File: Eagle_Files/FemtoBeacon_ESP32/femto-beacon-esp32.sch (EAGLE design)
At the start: 64 parts, among them IC1 FT232RQ

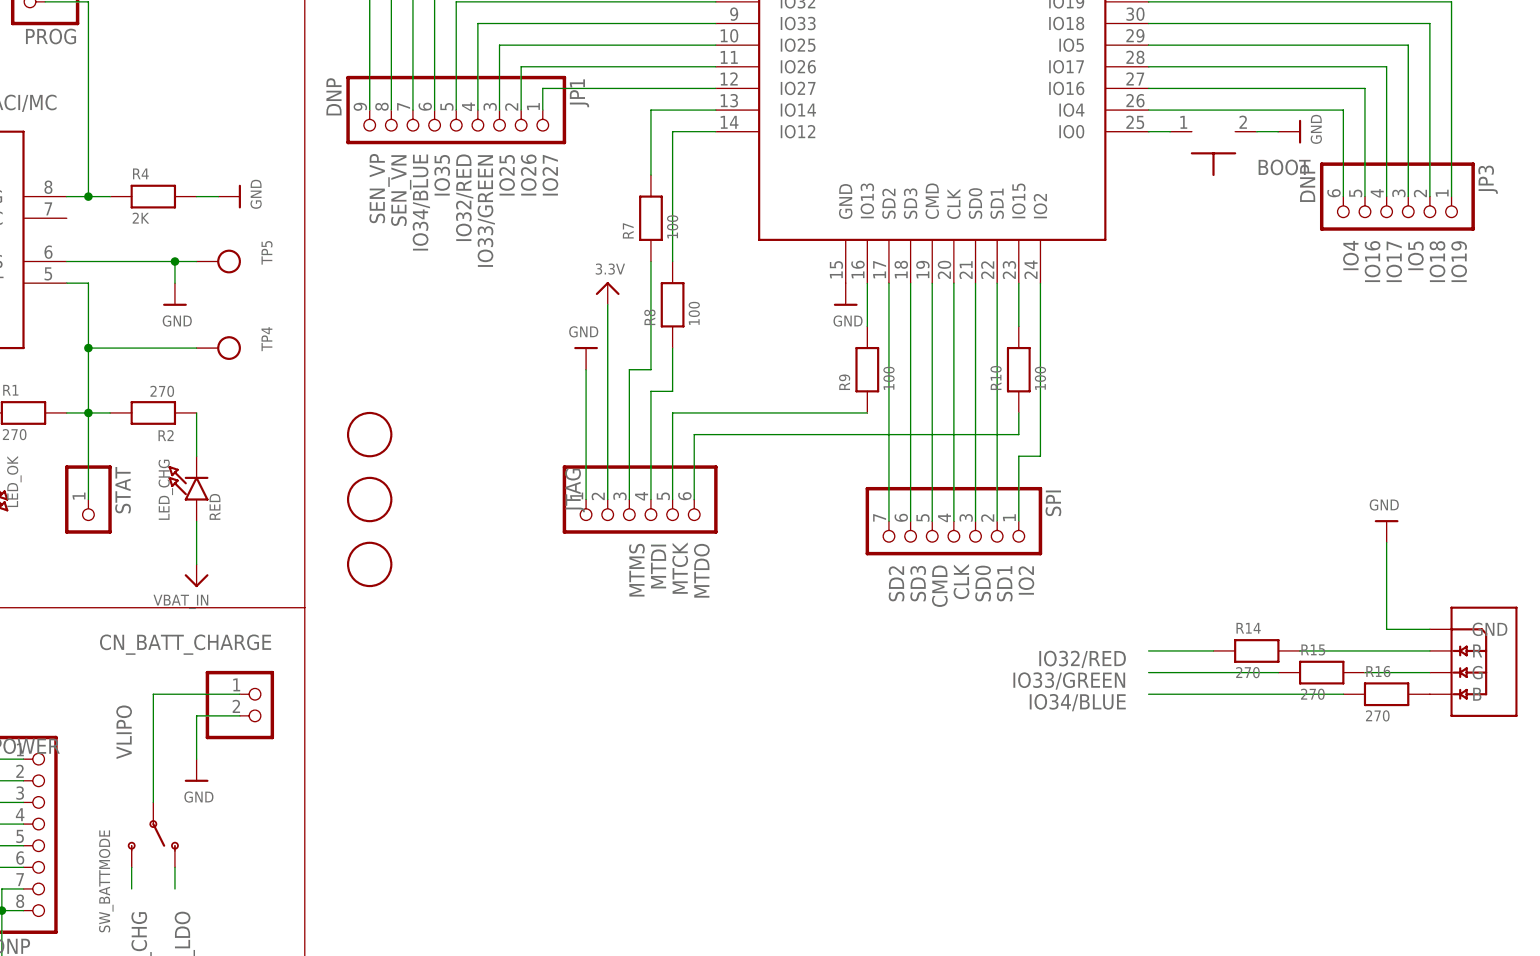
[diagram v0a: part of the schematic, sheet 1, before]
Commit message: Updating ESP32-WROOM-32 board. RGB Blue pin reassigned, and RGB pin 1 set to VCC instead of GND. LiPo connector pins were switched, corrected now.
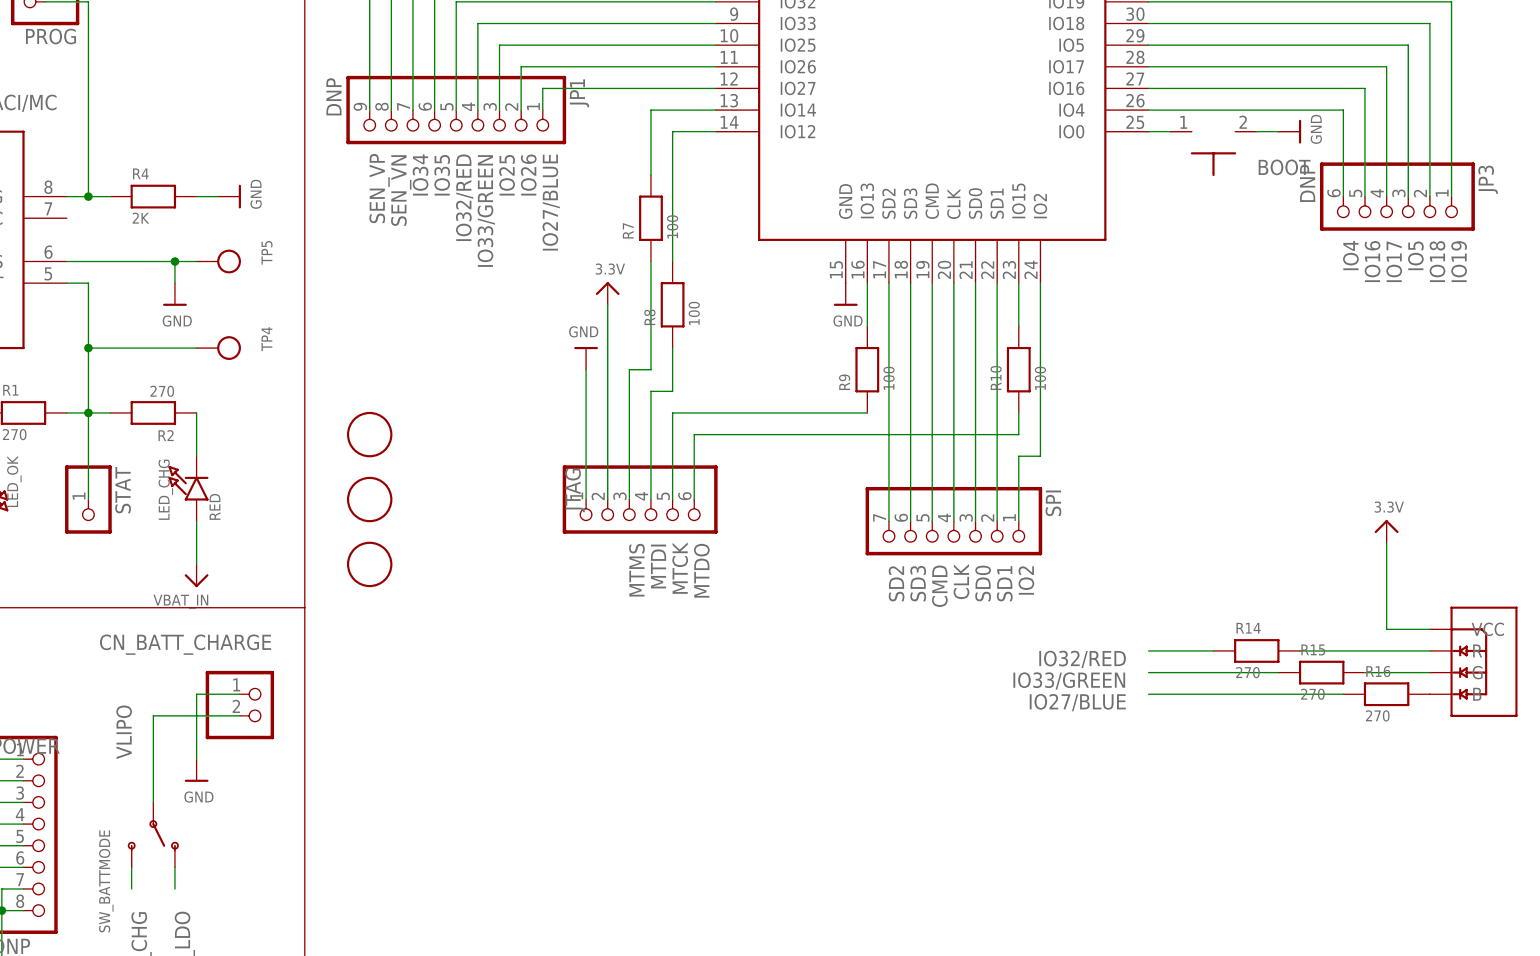
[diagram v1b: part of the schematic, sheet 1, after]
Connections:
- removed net IO27: JP1.1, MOD1.IO27
- removed net IO34/BLUE: JP1.7, MOD1.IO34, R16.1
- new net IO27/BLUE: JP1.1, MOD1.IO27, R16.1
- new net IO34: JP1.7, MOD1.IO34
- net GND: now also CN_BATT_CHARGE.1; no longer CN_BATT_CHARGE.2, RGB1.GND
- net VCC: now also RGB1.VCC
- net VLIPO: now also CN_BATT_CHARGE.2; no longer CN_BATT_CHARGE.1
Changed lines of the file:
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@@
 <grid distance="0.1" unitdist="inch" unit="inch" style="lines" multiple="1" display="no" altdistance="0.01" altunitdist="inch" altunit="inch"/>
 <layers>
-<layer number="1" name="Top" color="4" fill="1" visible="yes" active="no"/>
-<layer number="2" name="Route2" color="16" fill="1" visible="yes" active="no"/>
-<layer number="15" name="Route15" color="23" fill="1" visible="yes" active="no"/>
-<layer number="16" name="Bottom" color="1" fill="1" visible="yes" active="no"/>
-<layer number="17" name="Pads" color="2" fill="1" visible="yes" active="no"/>
-<layer number="18" name="Vias" color="2" fill="1" visible="yes" active="no"/>
-<layer number="19" name="Unrouted" color="6" fill="1" visible="yes" active="no"/>
-<layer number="20" name="Dimension" color="24" fill="1" visible="yes" active="no"/>
-<layer number="21" name="tPlace" color="7" fill="1" visible="yes" active="no"/>
-<layer number="22" name="bPlace" color="52" fill="1" visible="yes" active="no"/>
-<layer number="23" name="tOrigins" color="15" fill="1" visible="yes" active="no"/>
-<layer number="24" name="bOrigins" color="15" fill="1" visible="yes" active="no"/>
-<layer number="25" name="tNames" color="7" fill="1" visible="yes" active="no"/>
-<layer number="26" name="bNames" color="7" fill="1" visible="yes" active="no"/>
-<layer number="27" name="tValues" color="7" fill="1" visible="yes" active="no"/>
-<layer number="28" name="bValues" color="7" fill="1" visible="yes" active="no"/>
+<layer number="1" name="Top" color="4" fill="1" visible="no" active="no"/>
+<layer number="2" name="Route2" color="16" fill="1" visible="no" active="no"/>
+<layer number="15" name="Route15" color="23" fill="1" visible="no" active="no"/>
+<layer number="16" name="Bottom" color="1" fill="1" visible="no" active="no"/>
+<layer number="17" name="Pads" color="2" fill="1" visible="no" active="no"/>
+<layer number="18" name="Vias" color="2" fill="1" visible="no" active="no"/>
+<layer number="19" name="Unrouted" color="6" fill="1" visible="no" active="no"/>
+<layer number="20" name="Dimension" color="24" fill="1" visible="no" active="no"/>
+<layer number="21" name="tPlace" color="7" fill="1" visible="no" active="no"/>
+<layer number="22" name="bPlace" color="52" fill="1" visible="no" active="no"/>
+<layer number="23" name="tOrigins" color="15" fill="1" visible="no" active="no"/>
+<layer number="24" name="bOrigins" color="15" fill="1" visible="no" active="no"/>
+<layer number="25" name="tNames" color="7" fill="1" visible="no" active="no"/>
+<layer number="26" name="bNames" color="7" fill="1" visible="no" active="no"/>
+<layer number="27" name="tValues" color="7" fill="1" visible="no" active="no"/>
+<layer number="28" name="bValues" color="7" fill="1" visible="no" active="no"/>
 <layer number="29" name="tStop" color="7" fill="3" visible="no" active="no"/>
 <layer number="30" name="bStop" color="7" fill="6" visible="no" active="no"/>
@@
 <layer number="35" name="tGlue" color="7" fill="4" visible="no" active="no"/>
 <layer number="36" name="bGlue" color="7" fill="5" visible="no" active="no"/>
-<layer number="37" name="tTest" color="7" fill="1" visible="yes" active="no"/>
-<layer number="38" name="bTest" color="7" fill="1" visible="yes" active="no"/>
+<layer number="37" name="tTest" color="7" fill="1" visible="no" active="no"/>
+<layer number="38" name="bTest" color="7" fill="1" visible="no" active="no"/>
 <layer number="39" name="tKeepout" color="4" fill="11" visible="no" active="no"/>
 <layer number="40" name="bKeepout" color="1" fill="11" visible="no" active="no"/>
@@
 <layer number="44" name="Drills" color="7" fill="1" visible="no" active="no"/>
 <layer number="45" name="Holes" color="7" fill="1" visible="no" active="no"/>
-<layer number="46" name="Milling" color="3" fill="1" visible="yes" active="no"/>
-<layer number="47" name="Measures" color="7" fill="1" visible="yes" active="no"/>
-<layer number="48" name="Document" color="7" fill="1" visible="yes" active="no"/>
-<layer number="49" name="Reference" color="7" fill="1" visible="yes" active="no"/>
-<layer number="50" name="dxf" color="7" fill="1" visible="yes" active="no"/>
-<layer number="51" name="tDocu" color="7" fill="1" visible="yes" active="no"/>
-<layer number="52" name="bDocu" color="7" fill="1" visible="yes" active="no"/>
-<layer number="53" name="tGND_GNDA" color="7" fill="9" visible="yes" active="no"/>
-<layer number="54" name="bGND_GNDA" color="1" fill="9" visible="yes" active="no"/>
-<layer number="56" name="wert" color="7" fill="1" visible="yes" active="no"/>
-<layer number="57" name="tCAD" color="7" fill="1" visible="yes" active="no"/>
+<layer number="46" name="Milling" color="3" fill="1" visible="no" active="no"/>
+<layer number="47" name="Measures" color="7" fill="1" visible="no" active="no"/>
+<layer number="48" name="Document" color="7" fill="1" visible="no" active="no"/>
+<layer number="49" name="Reference" color="7" fill="1" visible="no" active="no"/>
+<layer number="50" name="dxf" color="7" fill="1" visible="no" active="no"/>
+<layer number="51" name="tDocu" color="7" fill="1" visible="no" active="no"/>
+<layer number="52" name="bDocu" color="7" fill="1" visible="no" active="no"/>
+<layer number="53" name="tGND_GNDA" color="7" fill="9" visible="no" active="no"/>
+<layer number="54" name="bGND_GNDA" color="1" fill="9" visible="no" active="no"/>
+<layer number="56" name="wert" color="7" fill="1" visible="no" active="no"/>
+<layer number="57" name="tCAD" color="7" fill="1" visible="no" active="no"/>
 <layer number="88" name="SimResults" color="9" fill="1" visible="yes" active="yes"/>
 <layer number="89" name="SimProbes" color="9" fill="1" visible="yes" active="yes"/>
@@
 <attribute name="MPN" value="CRCW0402270RFKED"/>
 </part>
-<part name="U$38" library="microbuilder" deviceset="GND" device=""/>
 <part name="CN1" library="microbuilder" deviceset="USB_TYPEA" device=""/>
 <part name="PROG" library="microbuilder" deviceset="HEADER-1X1" device="ROUND"/>
@@
 <part name="SJ3" library="microbuilder" deviceset="SOLDERJUMPER" device="CLOSED" value="DNP"/>
 <part name="U$30" library="microbuilder" deviceset="3.3V" device=""/>
+<part name="P+7" library="microbuilder" deviceset="VCC" device="" value="3.3V"/>
 </parts>
 <sheets>
@@
 <attribute name="MPN" x="228.6" y="40.64" size="1.778" layer="96" display="off"/>
 </instance>
-<instance part="U$38" gate="G$1" x="228.6" y="60.96" smashed="yes" rot="R180">
-<attribute name="VALUE" x="230.124" y="63.5" size="1.27" layer="96" rot="R180"/>
-</instance>
 <instance part="PROG" gate="G$1" x="68.58" y="121.92" smashed="yes" rot="R180">
 <attribute name="NAME" x="74.93" y="118.745" size="1.778" layer="95" rot="R180"/>
@@
 <instance part="U$43" gate="G$1" x="10.16" y="7.62" smashed="yes" rot="R270">
 <attribute name="VALUE" x="7.62" y="9.144" size="1.27" layer="96" rot="R270"/>
+</instance>
+<instance part="P+7" gate="VCC" x="228.6" y="60.96" smashed="yes">
+<attribute name="VALUE" x="227.076" y="61.976" size="1.27" layer="96"/>
 </instance>
 </instances>
@@
 </segment>
 <segment>
-<pinref part="CN_BATT_CHARGE" gate="G$1" pin="2"/>
-<wire x1="93.98" y1="38.1" x2="88.9" y2="38.1" width="0.1524" layer="91"/>
-<wire x1="88.9" y1="38.1" x2="88.9" y2="33.02" width="0.1524" layer="91"/>
+<wire x1="88.9" y1="40.64" x2="88.9" y2="33.02" width="0.1524" layer="91"/>
 <pinref part="U$18" gate="G$1" pin="GND"/>
-</segment>
-<segment>
-<pinref part="RGB1" gate="G$1" pin="GND"/>
-<wire x1="233.68" y1="48.26" x2="228.6" y2="48.26" width="0.1524" layer="91"/>
-<wire x1="228.6" y1="48.26" x2="228.6" y2="58.42" width="0.1524" layer="91"/>
-<pinref part="U$38" gate="G$1" pin="GND"/>
+<pinref part="CN_BATT_CHARGE" gate="G$1" pin="1"/>
+<wire x1="93.98" y1="40.64" x2="88.9" y2="40.64" width="0.1524" layer="91"/>
 </segment>
 <segment>
@@
 <wire x1="231.14" y1="165.1" x2="231.14" y2="152.4" width="0.1524" layer="91"/>
 <pinref part="P+6" gate="VCC" pin="VCC"/>
+</segment>
+<segment>
+<pinref part="RGB1" gate="G$1" pin="VCC"/>
+<wire x1="233.68" y1="48.26" x2="228.6" y2="48.26" width="0.1524" layer="91"/>
+<wire x1="228.6" y1="48.26" x2="228.6" y2="58.42" width="0.1524" layer="91"/>
+<pinref part="P+7" gate="VCC" pin="VCC"/>
 </segment>
 </net>
@@
 </segment>
 </net>
-<net name="IO34/BLUE" class="0">
+<net name="IO34" class="0">
 <segment>
 <pinref part="MOD1" gate="G$1" pin="IO34"/>
@@
 <pinref part="JP1" gate="A" pin="7"/>
 </segment>
-<segment>
-<pinref part="R16" gate="G$1" pin="1"/>
-<wire x1="223.52" y1="40.64" x2="200.66" y2="40.64" width="0.1524" layer="91"/>
-<label x="198.12" y="40.64" size="1.778" layer="95" rot="R180"/>
-</segment>
 </net>
 <net name="IO35" class="0">
@@
 </segment>
 </net>
-<net name="IO27" class="0">
+<net name="IO27/BLUE" class="0">
 <segment>
 <pinref part="MOD1" gate="G$1" pin="IO27"/>
@@
 <label x="129.54" y="104.14" size="1.778" layer="95" rot="R270"/>
 <pinref part="JP1" gate="A" pin="1"/>
+</segment>
+<segment>
+<pinref part="R16" gate="G$1" pin="1"/>
+<wire x1="223.52" y1="40.64" x2="200.66" y2="40.64" width="0.1524" layer="91"/>
+<label x="198.12" y="40.64" size="1.778" layer="95" rot="R180"/>
 </segment>
 </net>
@@
 <net name="VLIPO" class="0">
 <segment>
-<pinref part="CN_BATT_CHARGE" gate="G$1" pin="1"/>
-<wire x1="83.82" y1="40.64" x2="93.98" y2="40.64" width="0.1524" layer="91"/>
 <pinref part="SW_BATTMODE" gate="G$1" pin="P"/>
-<wire x1="83.82" y1="40.64" x2="83.82" y2="27.94" width="0.1524" layer="91"/>
 <label x="81.28" y="33.02" size="1.778" layer="95" rot="R90"/>
-</segment>
-</net>
+<pinref part="CN_BATT_CHARGE" gate="G$1" pin="2"/>
+<wire x1="83.82" y1="38.1" x2="83.82" y2="27.94" width="0.1524" layer="91"/>
+<wire x1="93.98" y1="38.1" x2="83.82" y2="38.1" width="0.1524" layer="91"/>
+</segment>
+</net>
